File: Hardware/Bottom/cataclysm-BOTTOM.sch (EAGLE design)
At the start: 0 parts

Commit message: Finished top and bottom schematic
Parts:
- added C1, C10, C11, C17, C18, C22: 100n, LinnesLab-Passives:CAPACITOR0603
- added C14, C19: 2.2n, LinnesLab-Passives:CAPACITOR0603
- added C15, C16: 2.2u, LinnesLab-Passives:CAPACITOR0603
- added C20: 22u, LinnesLab-Passives:CAPACITOR0603
- added C21: 22n, LinnesLab-Passives:CAPACITOR0603
- added IMU1: LSM6DS3_CAST, LinnesLab-Sensors:LSM6DS3_CAST
- added J1: (no value), LinnesLab-Connectors:CONN_07
- added OP3: (no value), LinnesLab-AnalogIC:OP-QUAD-SO14
- added OP4: (no value), LinnesLab-AnalogIC:OP-SINGLEOT
- added Q1: (no value), LinnesLab-DiscreteSemi:NPN-GENERIC
- added R13, R15, R19, R21: 220k, LinnesLab-Passives:RESISTOR0603
- added R14, R22: 10M, LinnesLab-Passives:RESISTOR0603
- added R16: (no value), LinnesLab-Passives:RESISTOR0603
- added R17, R18: 10k, LinnesLab-Passives:RESISTOR0402
- added R20, R23: 1M, LinnesLab-Passives:RESISTOR0603
- added R24: 10k, LinnesLab-Passives:RESISTOR0603
- added U$3: (no value), LinnesLab-Connectors:PPG.MODULE.2
- added U$4: AD5171, LinnesLab-DigitalIC:AD5171
- added U1: AD5242-SO16, LinnesLab-DigitalIC:AD5242-SO16
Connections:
- new net 3.3V: C1.2, C11.2, C17.2, C18.2, C22.2, IMU1.VCC, OP3G$5.V+, OP4G$2.V+, R13.2, R15.2, R17.2, U$3.V+, U$4.A0, U$4.VDD, U1.!SHDN, U1.VDD
- new net A6/TIA: C10.2, C15.1, J1.5, OP4G$1.OUT, U1.W1
- new net A7/PPG: C21.2, J1.7, OP3G$1.OUT
- new net D29/LED.CTRL: J1.6, U$4.A
- new net G.A1: U1.A1
- new net G.A2: U1.A2
- new net G.O1: U1.O1
- new net G.O2: U1.O2
- new net G.W2: C21.1, OP3G$1.-IN, R24.1, U1.W2
- new net GND: C1.1, C11.1, C17.1, C18.1, C22.1, IMU1.GND, OP3G$5.V-, OP4G$1.+IN, OP4G$2.V-, Q1.E, R18.1, R19.1, R21.1, U$3.GND, U$4.GND, U1.AD0, U1.AD1, U1.DGND, U1.VSS
- new net LED: Q1.C
- new net LED.C: U$3.LD1.C
- new net N$10: OP3G$4.+IN, R17.1, R18.2
- new net N$13: C15.2, OP3G$2.+IN, R13.1, R19.2
- new net N$15: C14.2, OP3G$2.-IN, R14.1, R20.2
- new net N$16: C14.1, C16.1, OP3G$2.OUT, R14.2
- new net N$17: C16.2, OP3G$3.+IN, R15.1, R21.2
- new net N$18: C19.2, OP3G$3.-IN, R22.1, R23.2
- new net N$19: C19.1, C20.1, OP3G$3.OUT, R22.2
- new net N$20: C20.2, R24.2
- new net N$4: J1.4
- new net N$5: J1.3
- new net N$6: J1.2
- new net N$7: J1.1
- new net N$8: Q1.B, R16.2
- new net N$9: R16.1, U$4.B, U$4.W
- new net PD.C: C10.1, OP4G$1.-IN, U$3.PD.C, U1.B1
- new net PPG: U1.B2
- new net SCL: IMU1.SCL, U$4.SCL, U1.SCL
- new net SDA: IMU1.SDA, U$4.SDA, U1.SDA
- new net VREF: OP3G$1.+IN, OP3G$4.-IN, OP3G$4.OUT, R20.1, R23.1
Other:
- note added: "Active Bandpass Filters"
- note added: "Digital Potentiometers"
- note added: "I2C Address: 0x2C"
- note added: "I2C Address: 0x2D"
- note added: "Photodiode and LEDs"
- note added: "Transimpedance Amplifier"

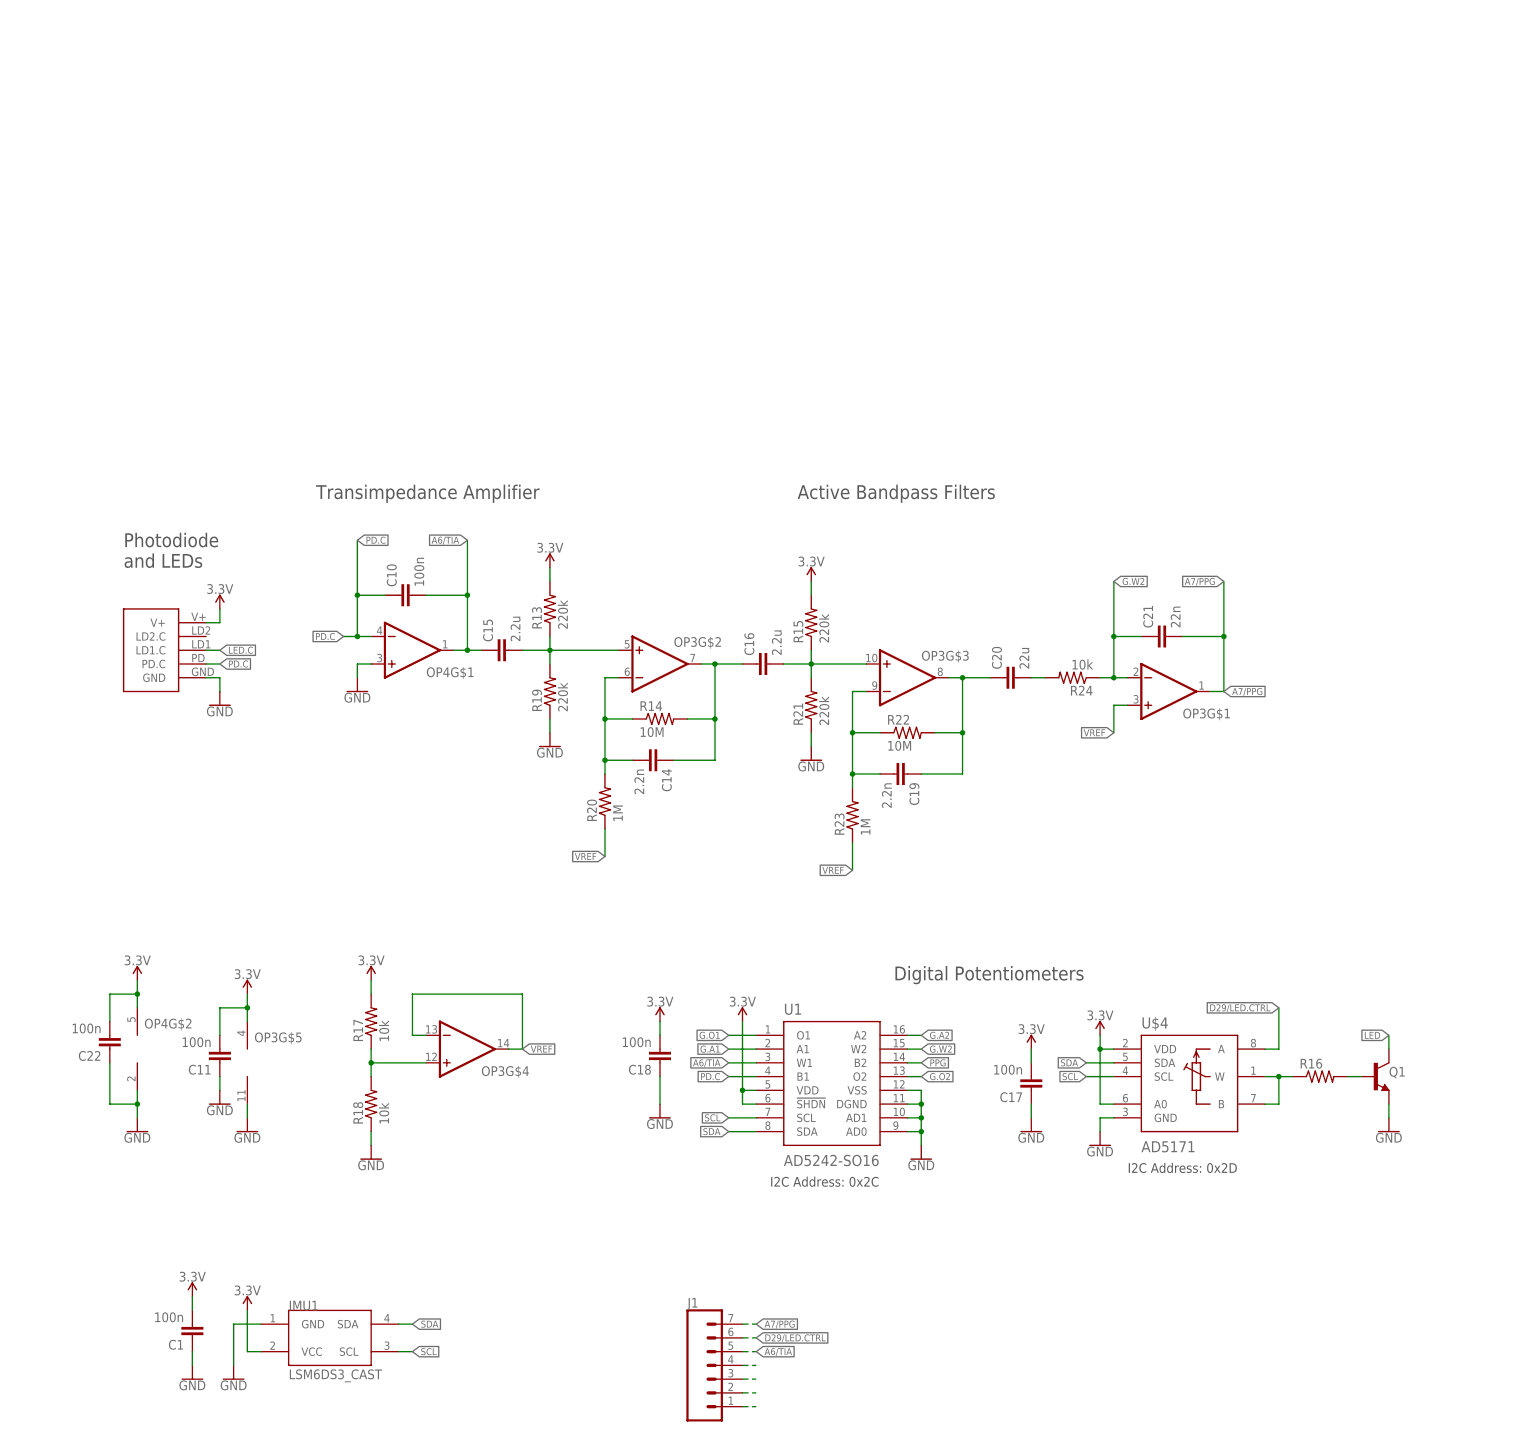
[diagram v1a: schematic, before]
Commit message: Routed bottom board
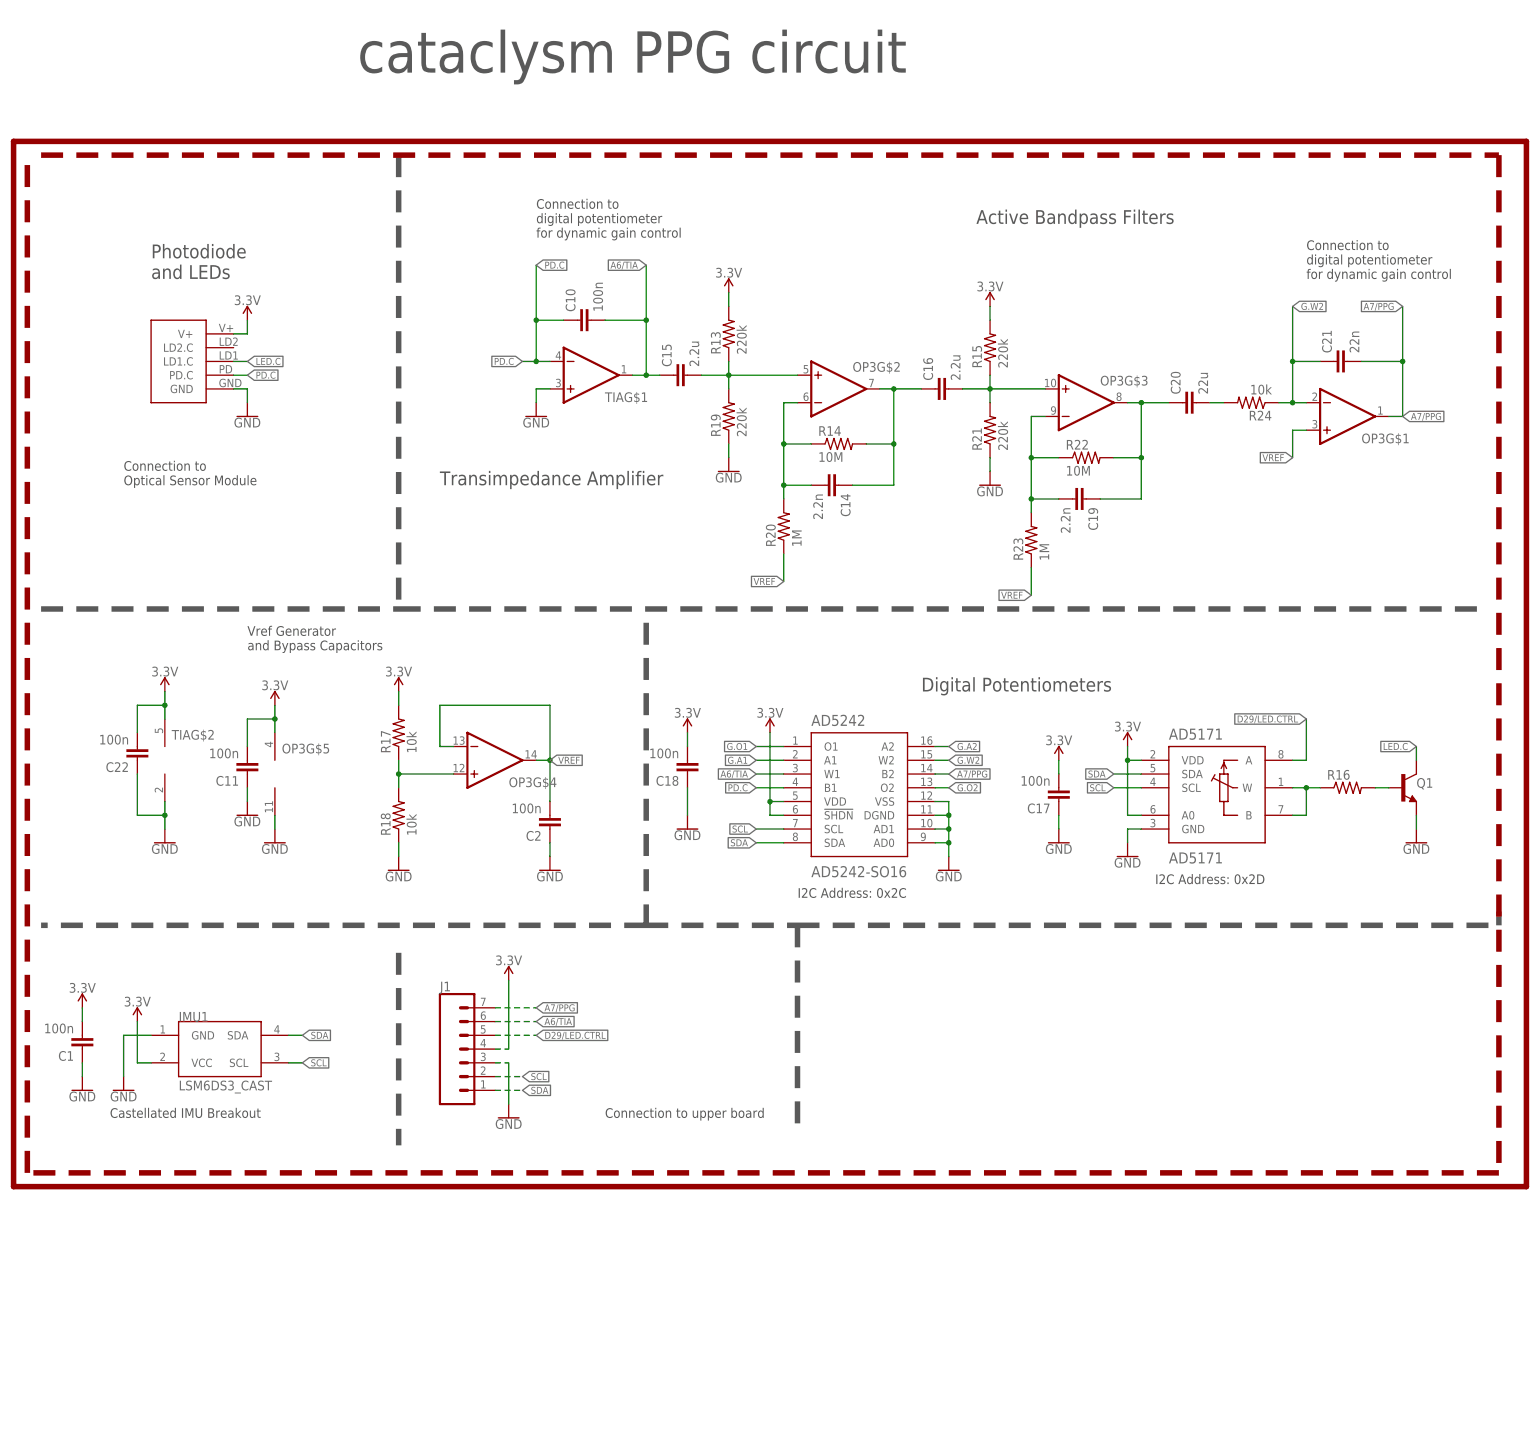
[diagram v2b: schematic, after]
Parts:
- removed OP4: (no value), LinnesLab-AnalogIC:OP-SINGLEOT
- removed U$4: AD5171, LinnesLab-DigitalIC:AD5171
- removed U1: AD5242-SO16, LinnesLab-DigitalIC:AD5242-SO16
- added AD5171: AD5171, LinnesLab-DigitalIC:AD5171
- added AD5242: AD5242-SO16, LinnesLab-DigitalIC:AD5242-SO16
- added C2: 100n, LinnesLab-Passives:CAPACITOR0603
- added LOGO1: REVISION.A, LinnesLab-Logos:REVISION.A
- added TIA: (no value), LinnesLab-AnalogIC:OP-SINGLEOT
- J1: device LinnesLab-Connectors:CONN_07 -> LinnesLab-Connectors:CONN_07-1.27MM
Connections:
- removed net LED: Q1.C
- removed net N$4: J1.4
- removed net N$5: J1.3
- removed net N$6: J1.2
- removed net N$7: J1.1
- removed net PPG: U1.B2
- net 3.3V: now also AD5171.A0, AD5171.VDD, AD5242.!SHDN, AD5242.VDD, J1.4, TIAG$2.V+; no longer OP4G$2.V+, U$4.A0, U$4.VDD, U1.!SHDN, U1.VDD
- net A6/TIA: now also AD5242.W1, J1.6, TIAG$1.OUT; no longer J1.5, OP4G$1.OUT, U1.W1
- net A7/PPG: now also AD5242.B2
- net D29/LED.CTRL: now also AD5171.A, J1.5; no longer J1.6, U$4.A
- net G.A1: now also AD5242.A1; no longer U1.A1
- net G.A2: now also AD5242.A2; no longer U1.A2
- net G.O1: now also AD5242.O1; no longer U1.O1
- net G.O2: now also AD5242.O2; no longer U1.O2
- net G.W2: now also AD5242.W2; no longer U1.W2
- net GND: now also AD5171.GND, AD5242.AD0, AD5242.AD1, AD5242.DGND, AD5242.VSS, C2.1, J1.3, TIAG$1.+IN, TIAG$2.V-; no longer OP4G$1.+IN, OP4G$2.V-, U$4.GND, U1.AD0, U1.AD1, U1.DGND, U1.VSS
- net LED.C: now also Q1.C
- net N$9: now also AD5171.B, AD5171.W; no longer U$4.B, U$4.W
- net PD.C: now also AD5242.B1, TIAG$1.-IN; no longer OP4G$1.-IN, U1.B1
- net SCL: now also AD5171.SCL, AD5242.SCL, J1.2; no longer U$4.SCL, U1.SCL
- net SDA: now also AD5171.SDA, AD5242.SDA, J1.1; no longer U$4.SDA, U1.SDA
- net VREF: now also C2.2
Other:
- note added: "Castellated IMU Breakout"
- note added: "Connection to Optical Sensor Module"
- note added: "Connection to digital potentiometer for dynamic gain control"
- note added: "Connection to upper board"
- note added: "Vref Generator and Bypass Capacitors"
- note added: "cataclysm PPG circuit"
- moved on the sheet: C1, C10, C11, C14, C15, C16, C17, C18, C19, C20, C21, C22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

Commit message: Almost finished with take 8
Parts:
- added C3, C4, C6: 1u, LinnesLab-Passives:CAPACITOR0603
- added C5, C8: 4.7u, LinnesLab-Passives:CAPACITOR0603
- added CHRG1: MCP73831, LinnesLab-Power:MCP73831
- added LDO1: MIC5504, LinnesLab-Power:MIC5504
- added R3: 100k, LinnesLab-Passives:RESISTOR0603
- added R4: (no value), LinnesLab-Passives:RESISTOR0603
- added U4: PCF8523, LinnesLab-Clocks:PCF8523
- added XTAL2: 32.7680kHz, LinnesLab-Clocks:CRYSTALECS-.327-12.5-12-C-TR
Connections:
- new net D27/CHRG.STATUS: CHRG1.STAT, R3.1
- new net N$1: U4.OSCO, XTAL2.1
- new net N$12: U4.OSCI, XTAL2.2
- new net N$14: CHRG1.PROG, R4.2
- new net VIN1: C4.2, C5.2, CHRG1.VIN, LDO1.EN, LDO1.IN, R3.2
- new net VLIPO: C8.1, CHRG1.VBAT
- net 3.3V: now also C3.1, C6.1, LDO1.OUT, U4.VDD
- net GND: now also C3.2, C4.1, C5.1, C6.2, C8.2, CHRG1.VSS, LDO1.GND, R4.1, U4.VSS
- net SCL: now also U4.SCL
- net SDA: now also U4.SDA
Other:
- note added: "Digital Output"
- note added: "I2C Address = 0x68h"
- note added: "Real-Time Clock"

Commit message: Finished take 8!
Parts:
- removed C4, C6: 1u, LinnesLab-Passives:CAPACITOR0603
- removed C5, C8: 4.7u, LinnesLab-Passives:CAPACITOR0603
- removed CHRG1: MCP73831, LinnesLab-Power:MCP73831
- removed LDO1: MIC5504, LinnesLab-Power:MIC5504
- removed R3: 100k, LinnesLab-Passives:RESISTOR0603
- removed R4: (no value), LinnesLab-Passives:RESISTOR0603
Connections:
- net A6/TIA renamed A5/TIA
- net A7/PPG renamed A4/PPG
- net D29/LED.CTRL renamed D30/LED.CTRL
- removed net D27/CHRG.STATUS: CHRG1.STAT, R3.1
- removed net N$14: CHRG1.PROG, R4.2
- removed net VIN1: C4.2, C5.2, CHRG1.VIN, LDO1.EN, LDO1.IN, R3.2
- removed net VLIPO: C8.1, CHRG1.VBAT
- net 3.3V: no longer C6.1, LDO1.OUT
- net GND: no longer C4.1, C5.1, C6.2, C8.2, CHRG1.VSS, LDO1.GND, R4.1
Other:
- note removed: "Digital Output"
- moved on the sheet: C3, U4, XTAL2
